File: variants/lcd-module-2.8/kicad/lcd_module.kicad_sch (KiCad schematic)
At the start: 1 part, among them J701 Pico-ResTouch-LCD-2.8

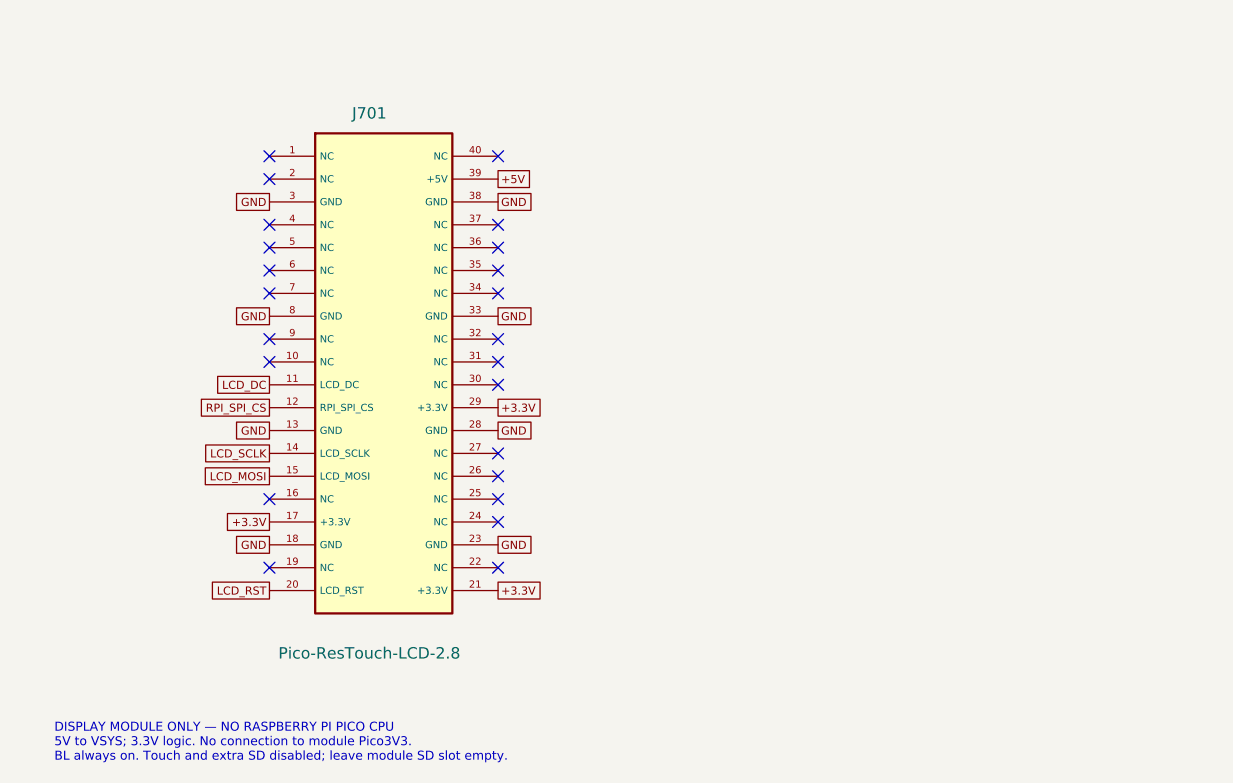
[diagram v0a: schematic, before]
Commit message: Rebuild modular signer as an eight-pin 2.8-inch pill carrier
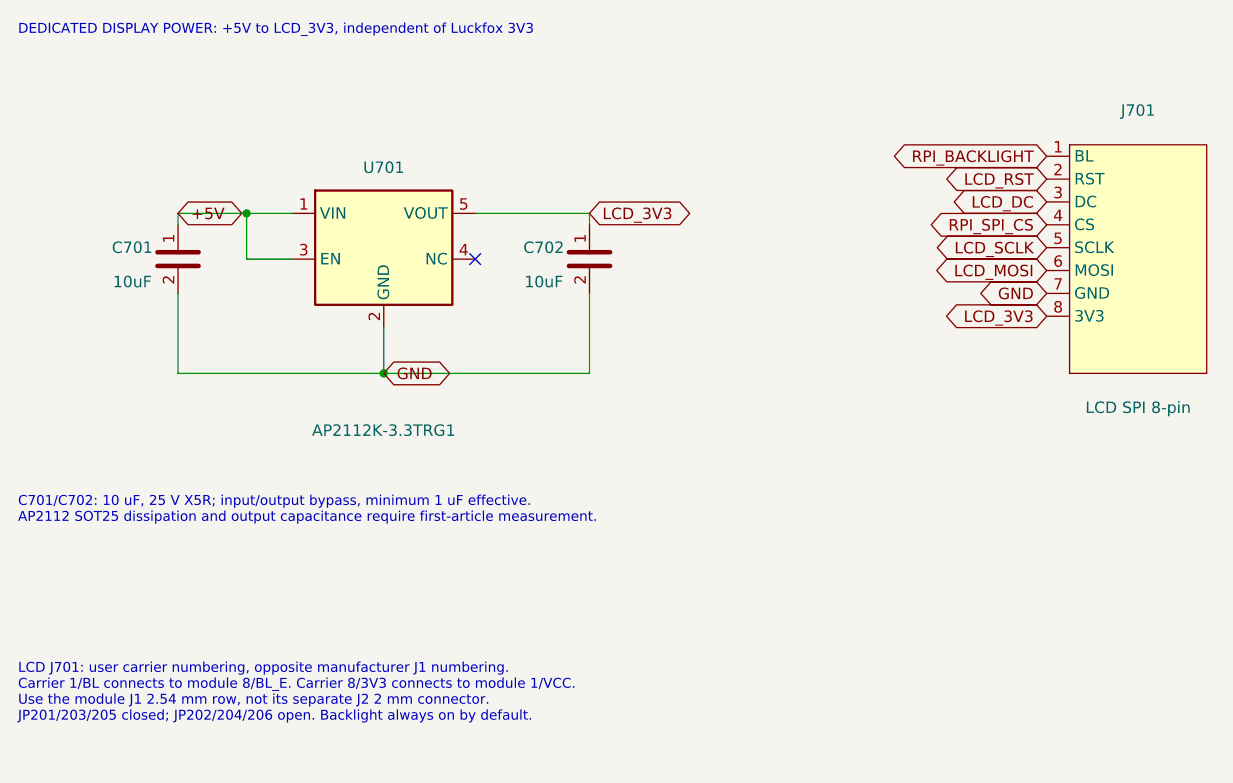
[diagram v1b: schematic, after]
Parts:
- added C701, C702: 10uF, Capacitor_SMD:C_0805_2012Metric_Pad1.18x1.45mm_HandSolder, symbol ShieldSigner:LCD_Cap
- added U701: AP2112K-3.3TRG1, ShieldSigner:AP2112K_SOT25_reflow, symbol ShieldSigner:AP2112_33
- J701: value Pico-ResTouch-LCD-2.8 -> LCD SPI 8-pin; footprint ShieldSigner:Waveshare_Pico_ResTouch_LCD_2.8_Header -> ShieldSigner:LCD_SPI_8_Pill; symbol ShieldSigner:LCD_Module_40 -> ShieldSigner:LCD_SPI_8
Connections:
- net +5V: now also C701.1, U701.1 (VIN), U701.3 (EN); no longer J701.39 (+5V)
- net GND: now also J701.7 (GND), C701.2, C702.2, U701.2 (GND); no longer J701.13 (GND), J701.18 (GND), J701.23 (GND), J701.28 (GND), J701.3 (GND), J701.33 (GND), J701.38 (GND), J701.8 (GND)
- net LCD_DC: now also J701.3 (DC); no longer J701.11 (LCD_DC)
- net LCD_MOSI: now also J701.6 (MOSI); no longer J701.15 (LCD_MOSI)
- net LCD_RST: now also J701.2 (RST); no longer J701.20 (LCD_RST)
- net LCD_SCLK: now also J701.5 (SCLK); no longer J701.14 (LCD_SCLK)
- net RPI_SPI_CS: now also J701.4 (CS); no longer J701.12 (RPI_SPI_CS)
- net RPI_BACKLIGHT: now reaches J701.1 (BL)
- removed net +3.3V: J701.17 (+3.3V), J701.21 (+3.3V), J701.29 (+3.3V)
- new net LCD_3V3: C702.1, J701.8 (3V3), U701.5 (VOUT)
- no-connect marks 23 -> 1
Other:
- note added: "C701/C702: 10 uF, 25 V X5R; input/output bypass, minimum 1 uF effective. AP2112 SOT25 dissipation and output capacitance require first-article measurement."
- note added: "DEDICATED DISPLAY POWER: +5V to LCD_3V3, independent of Luckfox 3V3"
- note added: "LCD J701: user carrier numbering, opposite manufacturer J1 numbering. Carrier 1/BL connects to module 8/BL_E. Carrier 8/3V3 connects to module 1/VCC. Use the module J1 2.54 mm row, not its separate J2 2 mm connector. JP201/203/205 closed; JP202/204/206 open. Backlight always on by default."
- note removed: "DISPLAY MODULE ONLY — NO RASPBERRY PI PICO CPU 5V to VSYS; 3.3V logic. No connection to module Pico3V3. BL always on. Touch and extra SD disabled; leave module SD slot empty."
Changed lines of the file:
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@@
-(kicad_sch (version 20260306) (generator "eeschema") (paper "A4")
-    (global_label "GND" (shape passive) (at 88.9 69.85 0) (effects (font (size 0.9 0.9)) (justify right)) (property "Intersheetrefs" "${INTERSHEET_REFS}" (at 87.3 70.95 0) (effects (font (size 1 1)) (hide yes))))(global_label "GND" (shape passive) (at 88.9 82.55 0) (effects (font (size 0.9 0.9)) (justify right)) (property "Intersheetrefs" "${INTERSHEET_REFS}" (at 87.3 83.65 0) (effects (font (size 1 1)) (hide yes))))(global_label "LCD_DC" (shape passive) (at 88.9 90.17 0) (effects (font (size 0.9 0.9)) (justify right)) (property "Intersheetrefs" "${INTERSHEET_REFS}" (at 87.3 91.27 0) (effects (font (size 1 1)) (hide yes))))(global_label "RPI_SPI_CS" (shape passive) (at 88.9 92.71 0) (effects (font (size 0.9 0.9)) (justify right)) (property "Intersheetrefs" "${INTERSHEET_REFS}" (at 87.3 93.81 0) (effects (font (size 1 1)) (hide yes))))(global_label "GND" (shape passive) (at 88.9 95.25 0) (effects (font (size 0.9 0.9)) (justify right)) (property "Intersheetrefs" "${INTERSHEET_REFS}" (at 87.3 96.35 0) (effects (font (size 1 1)) (hide yes))))(global_label "LCD_SCLK" (shape passive) (at 88.9 97.79 0) (effects (font (size 0.9 0.9)) (justify right)) (property "Intersheetrefs" "${INTERSHEET_REFS}" (at 87.3 98.89 0) (effects (font (size 1 1)) (hide yes))))(global_label "LCD_MOSI" (shape passive) (at 88.9 100.33 0) (effects (font (size 0.9 0.9)) (justify right)) (property "Intersheetrefs" "${INTERSHEET_REFS}" (at 87.3 101.43 0) (effects (font (size 1 1)) (hide yes))))(global_label "+3.3V" (shape passive) (at 88.9 105.41 0) (effects (font (size 0.9 0.9)) (justify right)) (property "Intersheetrefs" "${INTERSHEET_REFS}" (at 87.3 106.51 0) (effects (font (size 1 1)) (hide yes))))(global_label "GND" (shape passive) (at 88.9 107.95 0) (effects (font (size 0.9 0.9)) (justify right)) (property "Intersheetrefs" "${INTERSHEET_REFS}" (at 87.3 109.05 0) (effects (font (size 1 1)) (hide yes))))(global_label "LCD_RST" (shape passive) (at 88.9 113.03 0) (effects (font (size 0.9 0.9)) (justify right)) (property "Intersheetrefs" "${INTERSHEET_REFS}" (at 87.3 114.13 0) (effects (font (size 1 1)) (hide yes))))(global_label "+3.3V" (shape passive) (at 114.3 113.03 180) (effects (font (size 0.9 0.9)) (justify left)) (property "Intersheetrefs" "${INTERSHEET_REFS}" (at 112.7 114.13 180) (effects (font (size 1 1)) (hide yes))))(global_label "GND" (shape passive) (at 114.3 107.95 180) (effects (font (size 0.9 0.9)) (justify left)) (property "Intersheetrefs" "${INTERSHEET_REFS}" (at 112.7 109.05 180) (effects (font (size 1 1)) (hide yes))))(global_label "GND" (shape passive) (at 114.3 95.25 180) (effects (font (size 0.9 0.9)) (justify left)) (property "Intersheetrefs" "${INTERSHEET_REFS}" (at 112.7 96.35 180) (effects (font (size 1 1)) (hide yes))))(global_label "+3.3V" (shape passive) (at 114.3 92.71 180) (effects (font (size 0.9 0.9)) (justify left)) (property "Intersheetrefs" "${INTERSHEET_REFS}" (at 112.7 93.81 180) (effects (font (size 1 1)) (hide yes))))(global_label "GND" (shape passive) (at 114.3 82.55 180) (effects (font (size 0.9 0.9)) (justify left)) (property "Intersheetrefs" "${INTERSHEET_REFS}" (at 112.7 83.65 180) (effects (font (size 1 1)) (hide yes))))(global_label "GND" (shape passive) (at 114.3 69.85 180) (effects (font (size 0.9 0.9)) (justify left)) (property "Intersheetrefs" "${INTERSHEET_REFS}" (at 112.7 70.95 180) (effects (font (size 1 1)) (hide yes))))(global_label "+5V" (shape passive) (at 114.3 67.31 180) (effects (font (size 0.9 0.9)) (justify left)) (property "Intersheetrefs" "${INTERSHEET_REFS}" (at 112.7 68.41 180) (effects (font (size 1 1)) (hide yes))))(no_connect (at 88.9 64.77))(no_connect (at 88.9 67.31))(no_connect (at 88.9 72.39))(no_connect (at 88.9 74.93))(no_connect (at 88.9 77.47))(no_connect (at 88.9 80.01))(no_connect (at 88.9 85.09))(no_connect (at 88.9 87.63))(no_connect (at 88.9 102.87))(no_connect (at 88.9 110.49))(no_connect (at 114.3 110.49))(no_connect (at 114.3 105.41))(no_connect (at 114.3 102.87))(no_connect (at 114.3 100.33))(no_connect (at 114.3 97.79))(no_connect (at 114.3 90.17))(no_connect (at 114.3 87.63))(no_connect (at 114.3 85.09))(no_connect (at 114.3 80.01))(no_connect (at 114.3 77.47))(no_connect (at 114.3 74.93))(no_connect (at 114.3 72.39))(no_connect (at 114.3 64.77))
-    (text "DISPLAY MODULE ONLY — NO RASPBERRY PI PICO CPU\n5V to VSYS; 3.3V logic. No connection to module Pico3V3.\nBL always on. Touch and extra SD disabled; leave module SD slot empty." (at 65 130 0) (effects (font (size 1 1)) (justify left)))
-    (symbol (lib_id "ShieldSigner:LCD_Module_40") (at 101.6 88.9 0) (unit 1) (body_style 1) (in_bom yes) (on_board yes) (dnp no)
-    (property "Reference" "J701" (at 100 60 0) (effects (font (size 1.27 1.27))))
-    (property "Value" "Pico-ResTouch-LCD-2.8" (at 100 120 0) (effects (font (size 1.27 1.27))))
-    (property "Footprint" "ShieldSigner:Waveshare_Pico_ResTouch_LCD_2.8_Header" (at 100 90 0) (effects (font (size 1 1)) (hide yes)))
-    (pin "1")(pin "2")(pin "3")(pin "4")(pin "5")(pin "6")(pin "7")(pin "8")(pin "9")(pin "10")(pin "11")(pin "12")(pin "13")(pin "14")(pin "15")(pin "16")(pin "17")(pin "18")(pin "19")(pin "20")(pin "21")(pin "22")(pin "23")(pin "24")(pin "25")(pin "26")(pin "27")(pin "28")(pin "29")(pin "30")(pin "31")(pin "32")(pin "33")(pin "34")(pin "35")(pin "36")(pin "37")(pin "38")(pin "39")(pin "40") (instances (project "SeedSigner-Plus-smartcard-pico" (path "/8c9c54c8-0cfa-43ef-b1ba-3cda1bca877f/4fead130-596d-4414-bb04-d5dfc4d319ed" (reference "J701") (unit 1)))))
-    (embedded_fonts no))
